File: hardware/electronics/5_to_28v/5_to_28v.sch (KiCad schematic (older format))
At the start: 29 parts

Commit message: add changesto arduino and hardware
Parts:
- A?: symbol MCU_Module:Arduino_Nano_v3.x -> 5_to_28v-rescue:Arduino_Nano_v3.x-MCU_Module
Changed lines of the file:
@@
 EESchema Schematic File Version 4
-LIBS:5_to_28v-cache
 EELAYER 30 0
 EELAYER END
@@
 	2100 4800 2300 4800
 $Comp
-L MCU_Module:Arduino_Nano_v3.x A?
+L 5_to_28v-rescue:Arduino_Nano_v3.x-MCU_Module A?
 U 1 1 5DCCC149
 P 2500 2500

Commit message: add baords and updates to code
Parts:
- removed D? (x4): LED, symbol Device:LED
- removed R? (x4): R_Small, symbol Device:R_Small
- removed U?: LM2596T-5, Package_TO_SOT_THT:TO-220-5_P3.4x3.7mm_StaggerOdd_Lead3.8mm_Vertical, symbol Regulator_Switching:LM2596T-5
- removed U?: SFH617A-1X001, Package_DIP:DIP-4_W7.62mm, symbol Isolator:SFH617A-1X001
- added D2, D3: LED, LED_THT:LED_D5.0mm, symbol Device:LED
- added J2: Conn_Coaxial, Connector_Coaxial:BNC_Amphenol_B6252HB-NPP3G-50_Horizontal, symbol Connector:Conn_Coaxial
- added J3: output signal from med associates, symbol Connector:Conn_01x02_Female
- added J5: from_med_assoc_power, symbol Connector:Conn_01x02_Female
- added Q2: lickspout_sensor, LED_THT:LED_D5.0mm, symbol Device:Q_Photo_NPN
- added Q4: headentry_sensor, LED_THT:LED_D5.0mm, symbol Device:Q_Photo_NPN
- added R1, R6: 10k, symbol Device:R_Small
- added R10: 500, symbol Device:R_Small
- added R9: 3.5k, symbol Device:R_Small
- added RV1: lickspout_sensitivity, Potentiometer_THT:Potentiometer_ACP_CA6-H2,5_Horizontal, symbol Device:R_POT
- added U1: LM2596S-12, Package_TO_SOT_SMD:TO-263-5_TabPin3, symbol Regulator_Switching:LM2596S-12
- C1, C2: renamed from C?; footprint (none) -> Capacitor_THT:CP_Radial_D10.0mm_P5.00mm_P7.50mm
- D1: renamed from D?; footprint (none) -> Diode_THT:D_DO-27_P15.24mm_Horizontal
- L1: renamed from L?; value L -> 33µH
- gave numbers to parts that had none: 15
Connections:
- net +28V: now also C1.2, J5.1 (Pin_1); no longer J1.1 (Pin_1), J4.1 (Pin_1), Q3.3 (E), Q6.3 (E), R11.1, R5.1
- net GND: now also C2.2, D1.2 (A), D2.1 (K), D3.1 (K), J2.2 (Ext), J3.2 (Pin_2), J5.2 (Pin_2), R1.2, R10.2, R6.2, U1.3 (GND), U1.5 (~ON~/OFF); no longer R12.2, R7.2
- net at A1.16 (D13): now also R4.2; no longer R4.1
- net at A1.19 (A0): now also Q2.2 (E), R1.1
- net at A1.20 (A1): now also RV1.2
- net at A1.21 (A2): now also Q4.2 (E), R6.1
- net +5V: now reaches A1.27 (+5V)
- net +5V: now also Q2.1 (C), Q4.1 (C), RV1.1
- net at A1.30 (VIN): now also C2.1, L1.2, U1.4 (FB)
- net at C1.1: now also U1.1 (VIN)
- net at D1.1 (K): now also L1.1, U1.2 (OUT)
- net at Q5.2 (B): now also R4.1; no longer R4.2
- new net: J1.1 (Pin_1), Q3.3 (E), R5.1
- new net: D2.2 (A), R7.2
- new net: D3.2 (A), R12.2
- new net: J4.1 (Pin_1), Q6.3 (E), R11.1
- new net: J3.1 (Pin_1), R9.1
- new net: J2.1 (In), R10.1, R9.2
- no-connect marks 0 -> 20
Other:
- note removed: "add for houselight?\n"
- moved on the sheet: A1, C1, C2, D1, J1, J4, L1, Q1, Q3, Q5, Q6, R11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

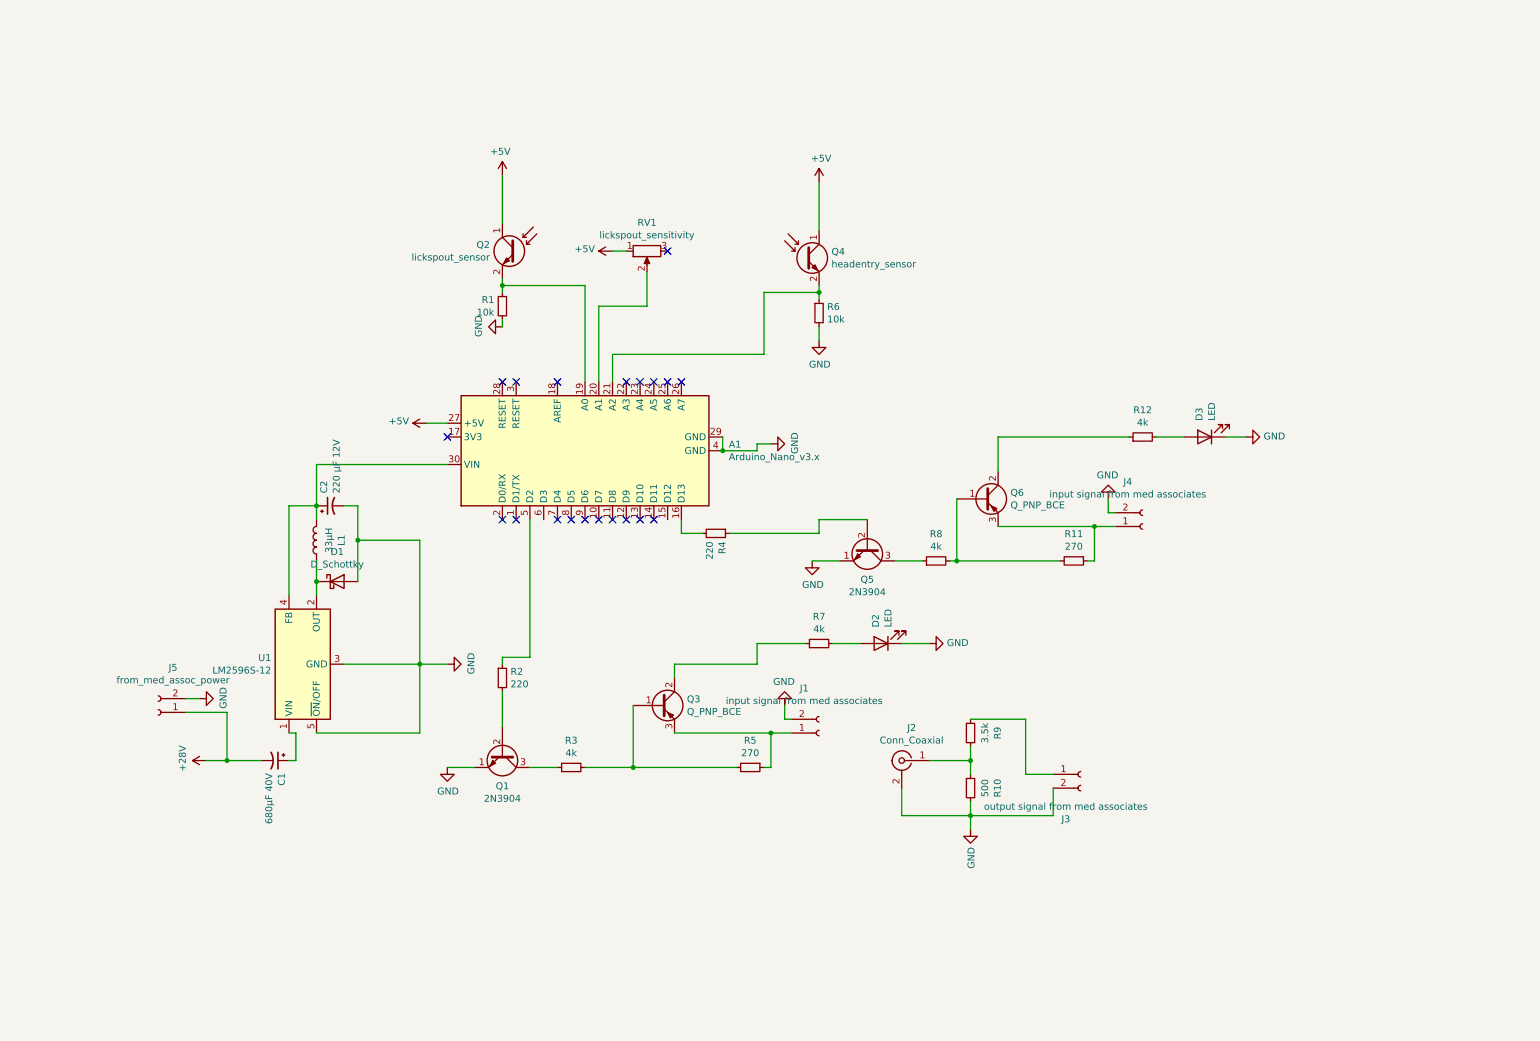
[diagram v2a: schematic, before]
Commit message: first implementation of a generic solution
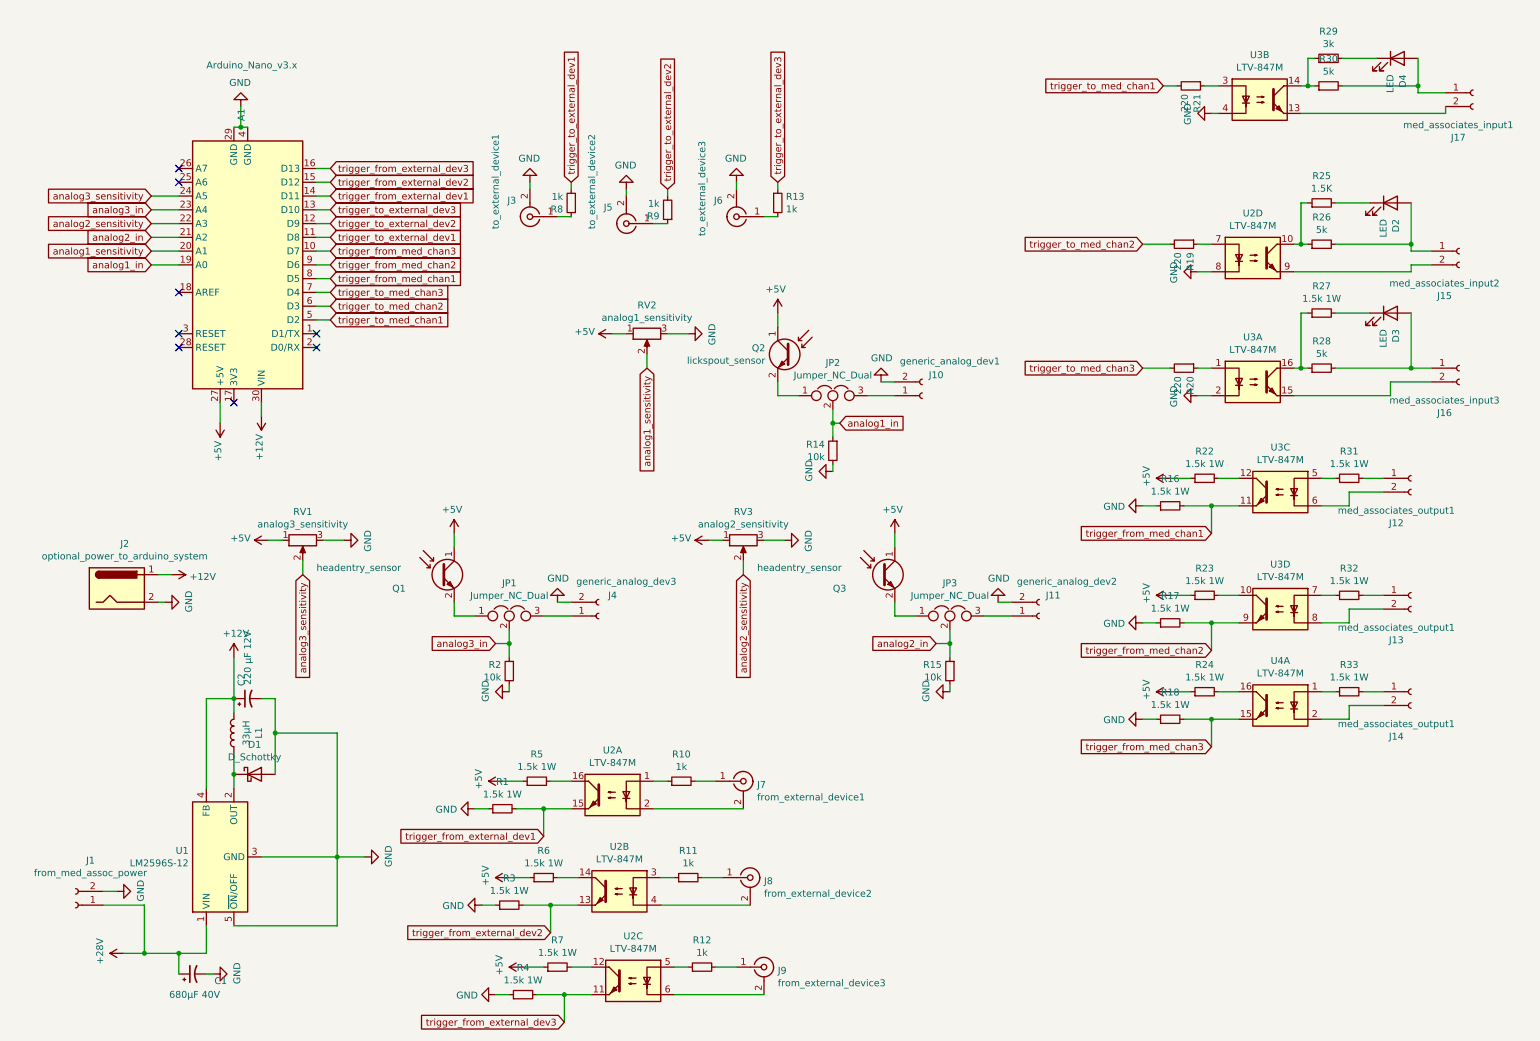
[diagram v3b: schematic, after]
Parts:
- removed J2: Conn_Coaxial, Connector_Coaxial:BNC_Amphenol_B6252HB-NPP3G-50_Horizontal, symbol Connector:Conn_Coaxial
- removed J3: output signal from med associates, symbol Connector:Conn_01x02_Female
- removed Q1, Q5: 2N3904, Package_TO_SOT_THT:TO-92_Inline, symbol Transistor_BJT:2N3904
- removed Q3, Q6: Q_PNP_BCE, symbol Device:Q_PNP_BCE
- added D3: LED, LED_THT:LED_D5.0mm, symbol Device:LED
- added J10: generic_analog_dev1, Connector_JST:JST_XH_B2B-XH-A_1x02_P2.50mm_Vertical, symbol Connector:Conn_01x02_Female
- added J11: generic_analog_dev2, Connector_JST:JST_XH_B2B-XH-A_1x02_P2.50mm_Vertical, symbol Connector:Conn_01x02_Female
- added J12, J13, J14: med_associates_output1, Connector_JST:JST_XH_B2B-XH-A_1x02_P2.50mm_Vertical, symbol Connector:Conn_01x02_Female
- added J16: med_associates_input3, Connector_JST:JST_XH_B2B-XH-A_1x02_P2.50mm_Vertical, symbol Connector:Conn_01x02_Female
- added J2: optional_power_to_arduino_system, Connector_BarrelJack:BarrelJack_Horizontal, symbol Connector:Barrel_Jack
- added J3: to_external_device1, Connector_JST:JST_XH_B2B-XH-A_1x02_P2.50mm_Vertical, symbol Connector:Conn_Coaxial
- added J4: generic_analog_dev3, Connector_JST:JST_XH_B2B-XH-A_1x02_P2.50mm_Vertical, symbol Connector:Conn_01x02_Female
- added J5: to_external_device2, Connector_JST:JST_XH_B2B-XH-A_1x02_P2.50mm_Vertical, symbol Connector:Conn_Coaxial
- added J6: to_external_device3, Connector_JST:JST_XH_B2B-XH-A_1x02_P2.50mm_Vertical, symbol Connector:Conn_Coaxial
- added J7: from_external_device1, Connector_JST:JST_XH_B2B-XH-A_1x02_P2.50mm_Vertical, symbol Connector:Conn_Coaxial
- added J8: from_external_device2, Connector_JST:JST_XH_B2B-XH-A_1x02_P2.50mm_Vertical, symbol Connector:Conn_Coaxial
- added J9: from_external_device3, Connector_JST:JST_XH_B2B-XH-A_1x02_P2.50mm_Vertical, symbol Connector:Conn_Coaxial
- added JP1, JP2, JP3: Jumper_NC_Dual, Connector_PinHeader_2.54mm:PinHeader_1x03_P2.54mm_Vertical, symbol Device:Jumper_NC_Dual
- added Q1: headentry_sensor, LED_THT:LED_D5.0mm, symbol Device:Q_Photo_NPN
- added R1, R16, R17, R18, R22, R23, R24, R27, R3, R31, R32, R33, R4: 1.5k 1W, Resistor_THT:R_Axial_DIN0516_L15.5mm_D5.0mm_P25.40mm_Horizontal, symbol Device:R_Small
- added R13, R8: 1k, Resistor_THT:R_Axial_DIN0411_L9.9mm_D3.6mm_P15.24mm_Horizontal, symbol Device:R_Small
- added R15, R2: 10k, Resistor_THT:R_Axial_DIN0516_L15.5mm_D5.0mm_P25.40mm_Horizontal, symbol Device:R_Small
- added R20: 220, Resistor_THT:R_Axial_DIN0411_L9.9mm_D3.6mm_P15.24mm_Horizontal, symbol Device:R_Small
- added R25: 1.5K, Resistor_THT:R_Axial_DIN0516_L15.5mm_D5.0mm_P25.40mm_Horizontal, symbol Device:R_Small
- added R28: 5k, Resistor_THT:R_Axial_DIN0516_L15.5mm_D5.0mm_P25.40mm_Horizontal, symbol Device:R_Small
- added R29: 3k, Resistor_THT:R_Axial_DIN0516_L15.5mm_D5.0mm_P25.40mm_Horizontal, symbol Device:R_Small
- added RV1: analog3_sensitivity, Connector_JST:JST_XH_B3B-XH-A_1x03_P2.50mm_Vertical, symbol Device:R_POT
- added RV3: analog2_sensitivity, Connector_JST:JST_XH_B3B-XH-A_1x03_P2.50mm_Vertical, symbol Device:R_POT
- added U2, U3, U4: LTV-847M, Package_DIP:DIP-16_W10.16mm, symbol Isolator:LTV-847M
- J1: renamed from J5; footprint (none) -> Connector_JST:JST_XH_B2B-XH-A_1x02_P2.50mm_Vertical
- J15: renamed from J1; value input signal from med associates -> med_associates_input2; footprint (none) -> Connector_JST:JST_XH_B2B-XH-A_1x02_P2.50mm_Vertical
- J17: renamed from J4; value input signal from med associates -> med_associates_input1; footprint (none) -> Connector_JST:JST_XH_B2B-XH-A_1x02_P2.50mm_Vertical
- L1: footprint (none) -> Inductor_THT:L_Radial_D7.5mm_P3.50mm_Fastron_07P
- R10: value 500 -> 1k; footprint (none) -> Resistor_THT:R_Axial_DIN0411_L9.9mm_D3.6mm_P15.24mm_Horizontal
- R11: value 270 -> 1k; footprint (none) -> Resistor_THT:R_Axial_DIN0411_L9.9mm_D3.6mm_P15.24mm_Horizontal
- R12: value 4k -> 1k; footprint (none) -> Resistor_THT:R_Axial_DIN0411_L9.9mm_D3.6mm_P15.24mm_Horizontal
- R14: renamed from R1; footprint (none) -> Resistor_THT:R_Axial_DIN0516_L15.5mm_D5.0mm_P25.40mm_Horizontal
- R19: renamed from R2; footprint (none) -> Resistor_THT:R_Axial_DIN0411_L9.9mm_D3.6mm_P15.24mm_Horizontal
- R21: renamed from R4; footprint (none) -> Resistor_THT:R_Axial_DIN0411_L9.9mm_D3.6mm_P15.24mm_Horizontal
- R26: renamed from R3; value 4k -> 5k; footprint (none) -> Resistor_THT:R_Axial_DIN0516_L15.5mm_D5.0mm_P25.40mm_Horizontal
- R30: renamed from R8; value 4k -> 5k; footprint (none) -> Resistor_THT:R_Axial_DIN0516_L15.5mm_D5.0mm_P25.40mm_Horizontal
- R5: value 270 -> 1.5k 1W; footprint (none) -> Resistor_THT:R_Axial_DIN0516_L15.5mm_D5.0mm_P25.40mm_Horizontal
- R6: value 10k -> 1.5k 1W; footprint (none) -> Resistor_THT:R_Axial_DIN0516_L15.5mm_D5.0mm_P25.40mm_Horizontal
- R7: value 4k -> 1.5k 1W; footprint (none) -> Resistor_THT:R_Axial_DIN0516_L15.5mm_D5.0mm_P25.40mm_Horizontal
- R9: value 3.5k -> 1k; footprint (none) -> Resistor_THT:R_Axial_DIN0411_L9.9mm_D3.6mm_P15.24mm_Horizontal
- RV2: renamed from RV1; value lickspout_sensitivity -> analog1_sensitivity; footprint Potentiometer_THT:Potentiometer_ACP_CA6-H2,5_Horizontal -> Connector_JST:JST_XH_B3B-XH-A_1x03_P2.50mm_Vertical
- U1: footprint Package_TO_SOT_SMD:TO-263-5_TabPin3 -> Package_TO_SOT_THT:TO-220-5_P3.4x3.7mm_StaggerOdd_Lead3.8mm_Vertical
- renumbered D3 to D4, Q4 to Q3
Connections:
- net +28V: now also C1.1, U1.1 (VIN); no longer C1.2
- net +5V: now also R5.1, R6.1, R7.1, Q1.1 (C), R22.1, R23.1, R24.1, RV1.1, RV3.1
- net GND: now also C1.2, RV2.3, J10.2 (Pin_2), J11.2 (Pin_2), J2.2, J3.2 (Ext), J4.2 (Pin_2), J5.2 (Ext), J6.2 (Ext), R1.1, R15.2, R16.1, R17.1, R18.1, R2.2, R3.1, R4.1, RV1.3, RV3.3, U2.8, U3.2, U3.4; no longer D2.1 (K), D4.1 (K), J15.2 (Pin_2), J17.2 (Pin_2), R10.2, R6.2
- net at R26.1: now also R25.1, U2.10
- net at R26.2: now also D2.2 (A), J15.1 (Pin_1); no longer R5.2
- net at R19.1: now also U2.7; no longer A1.5 (D2)
- net trigger_to_med_chan2: now reaches R19.2
- net trigger_to_med_chan2: now also A1.6 (D3)
- net at R7.2: now also U2.12; no longer D2.2 (A)
- net trigger_from_med_chan3: now reaches A1.10 (D7)
- net trigger_from_med_chan3: now also R18.2, U4.15
- net trigger_to_external_dev1: now reaches A1.11 (D8)
- net trigger_to_external_dev1: now also R8.2
- net trigger_to_external_dev2: now reaches A1.12 (D9)
- net trigger_to_external_dev2: now also R9.2
- net trigger_to_external_dev3: now reaches A1.13 (D10)
- net trigger_to_external_dev3: now also R13.1
- net trigger_from_external_dev1: now reaches A1.14 (D11)
- net trigger_from_external_dev1: now also R1.2, U2.15
- net trigger_from_external_dev2: now reaches A1.15 (D12)
- net trigger_from_external_dev2: now also R3.2, U2.13
- net trigger_from_external_dev3: now reaches A1.16 (D13)
- net trigger_from_external_dev3: now also R4.2, U2.11; no longer R21.2
- net analog1_in: now reaches A1.19 (A0), R14.1
- net analog1_in: now also JP2.2; no longer Q2.2 (E)
- net analog1_sensitivity: now reaches A1.20 (A1), RV2.2
- net analog2_sensitivity: now reaches A1.22 (A3)
- net analog2_sensitivity: now also RV3.2
- net analog3_in: now reaches A1.23 (A4)
- net analog3_in: now also JP1.2, R2.1
- net analog3_sensitivity: now reaches A1.24 (A5)
- net analog3_sensitivity: now also RV1.2
- net +12V: now reaches A1.30 (VIN), C2.1, L1.2, U1.4 (FB)
- net +12V: now also J2.1
- net trigger_to_med_chan3: now reaches A1.7 (D4)
- net trigger_to_med_chan3: now also R20.2
- net trigger_from_med_chan1: now reaches A1.8 (D5)
- net trigger_from_med_chan1: now also R16.2, U3.11
- net trigger_from_med_chan2: now reaches A1.9 (D6)
- net trigger_from_med_chan2: now also R17.2, U3.9
- net at R21.1: now also U3.3
- net at R12.1: now also U2.5
- net at D4.2 (A): now also J17.1 (Pin_1), R30.2; no longer R12.2
- net at R11.1: now also U2.3; no longer J17.1 (Pin_1)
- net at R11.2: now also J8.1 (In); no longer R30.2
- net at R30.1: now also R29.1, U3.14
- net at R9.1: now also J5.1 (In)
- net at R10.1: now also U2.1; no longer R9.2
- new net: J15.2 (Pin_2), U2.9
- new net: J17.2 (Pin_2), U3.13
- new net: JP2.1, Q2.2 (E)
- new net: JP3.1, Q3.2 (E)
- new net: D2.1 (K), R25.2
- new net: D4.1 (K), R29.2
- new net: D3.2 (A), J16.1 (Pin_1), R28.2
- new net: J16.2 (Pin_2), U3.15
- new net: R27.1, R28.1, U3.16
- new net: D3.1 (K), R27.2
- new net: R20.1, U3.1
- new net: R22.2, U3.12
- new net: R31.1, U3.5
- new net: J12.2 (Pin_2), U3.6
- new net: J12.1 (Pin_1), R31.2
- new net: R23.2, U3.10
- new net: R32.1, U3.7
- new net: J13.2 (Pin_2), U3.8
- new net: J13.1 (Pin_1), R32.2
- new net: R33.1, U4.1
- new net: R24.2, U4.16
- new net: J14.2 (Pin_2), U4.2
- new net: J14.1 (Pin_1), R33.2
- new net: R5.2, U2.16
- new net: J7.2 (Ext), U2.2
- new net: J7.1 (In), R10.2
- new net: R6.2, U2.14
- new net: J8.2 (Ext), U2.4
- new net: J9.2 (Ext), U2.6
- new net: J9.1 (In), R12.2
- new net: J3.1 (In), R8.1
- new net: J6.1 (In), R13.2
- new net: J10.1 (Pin_1), JP2.3
- new net: J11.1 (Pin_1), JP3.3
- new net: JP1.1, Q1.2 (E)
- new net: J4.1 (Pin_1), JP1.3
- new net analog2_in: A1.21 (A2), JP3.2, R15.1
- new net trigger_to_med_chan1: A1.5 (D2), R21.2
- no-connect marks 20 -> 8
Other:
- moved on the sheet: A1, C1, C2, D1, D2, D4, J1, J15, J17, L1, Q2, Q3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
